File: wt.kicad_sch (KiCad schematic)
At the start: 59 parts, among them J1 USB_B, J2 Conn_ARM_JTAG_SWD_20, U1 STM32F407VGTx, Y1 Crystal_8Mhz

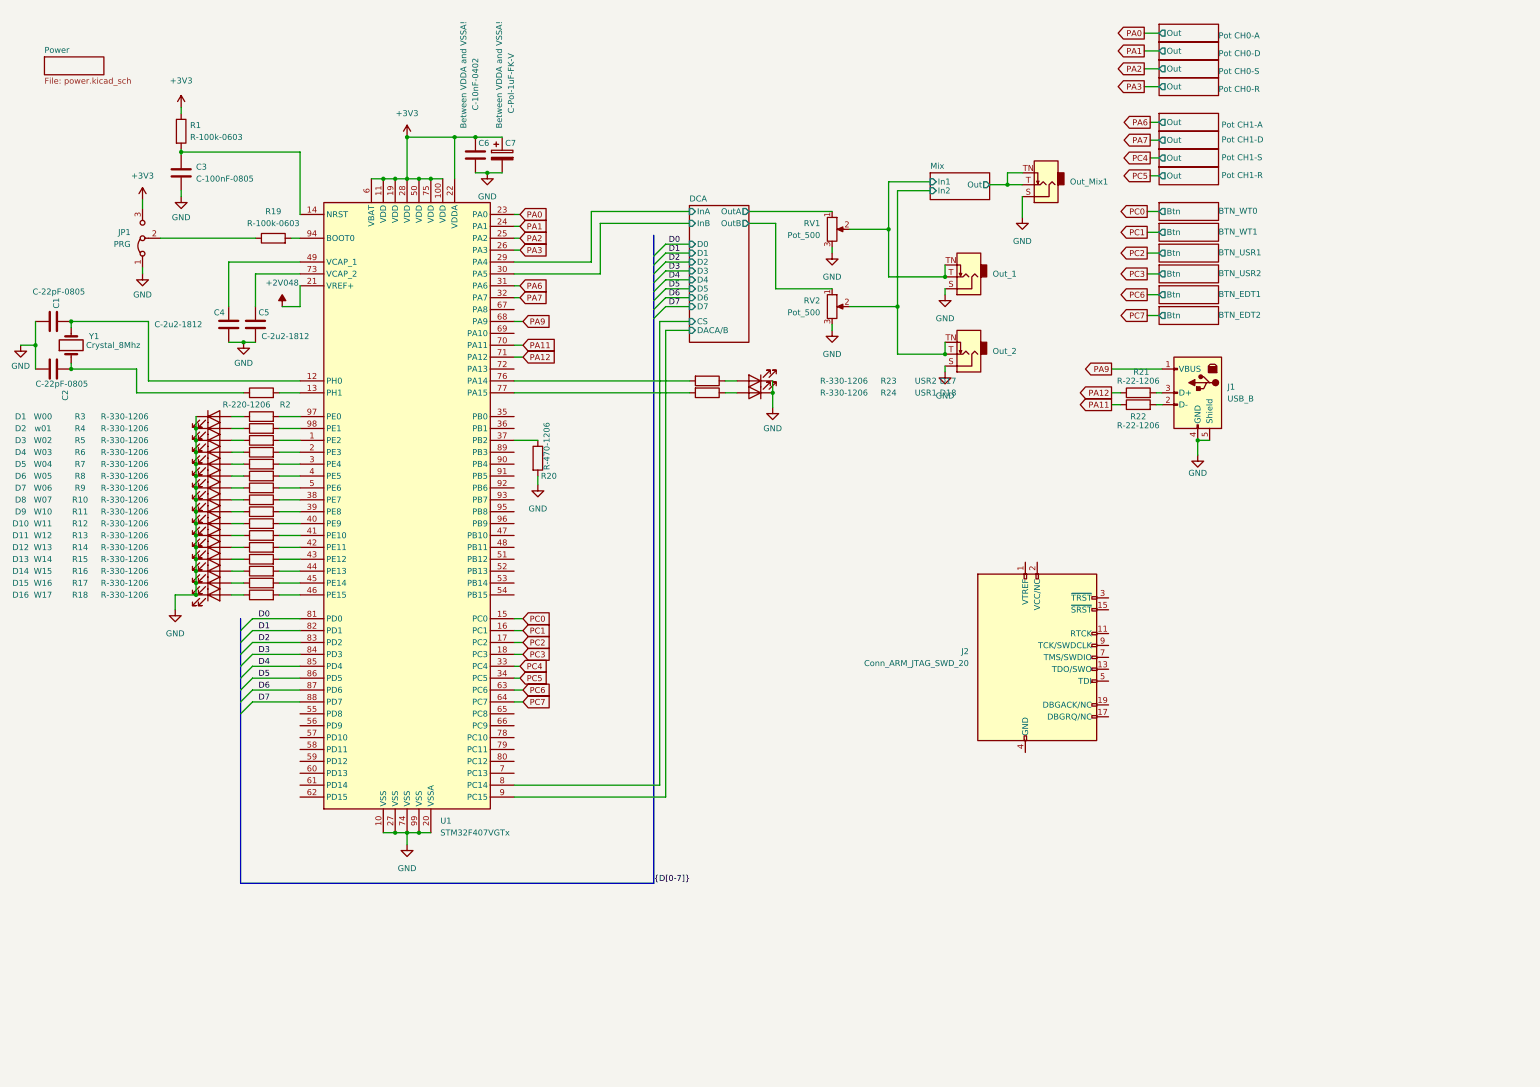
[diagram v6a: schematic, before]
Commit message: cleaning into modules
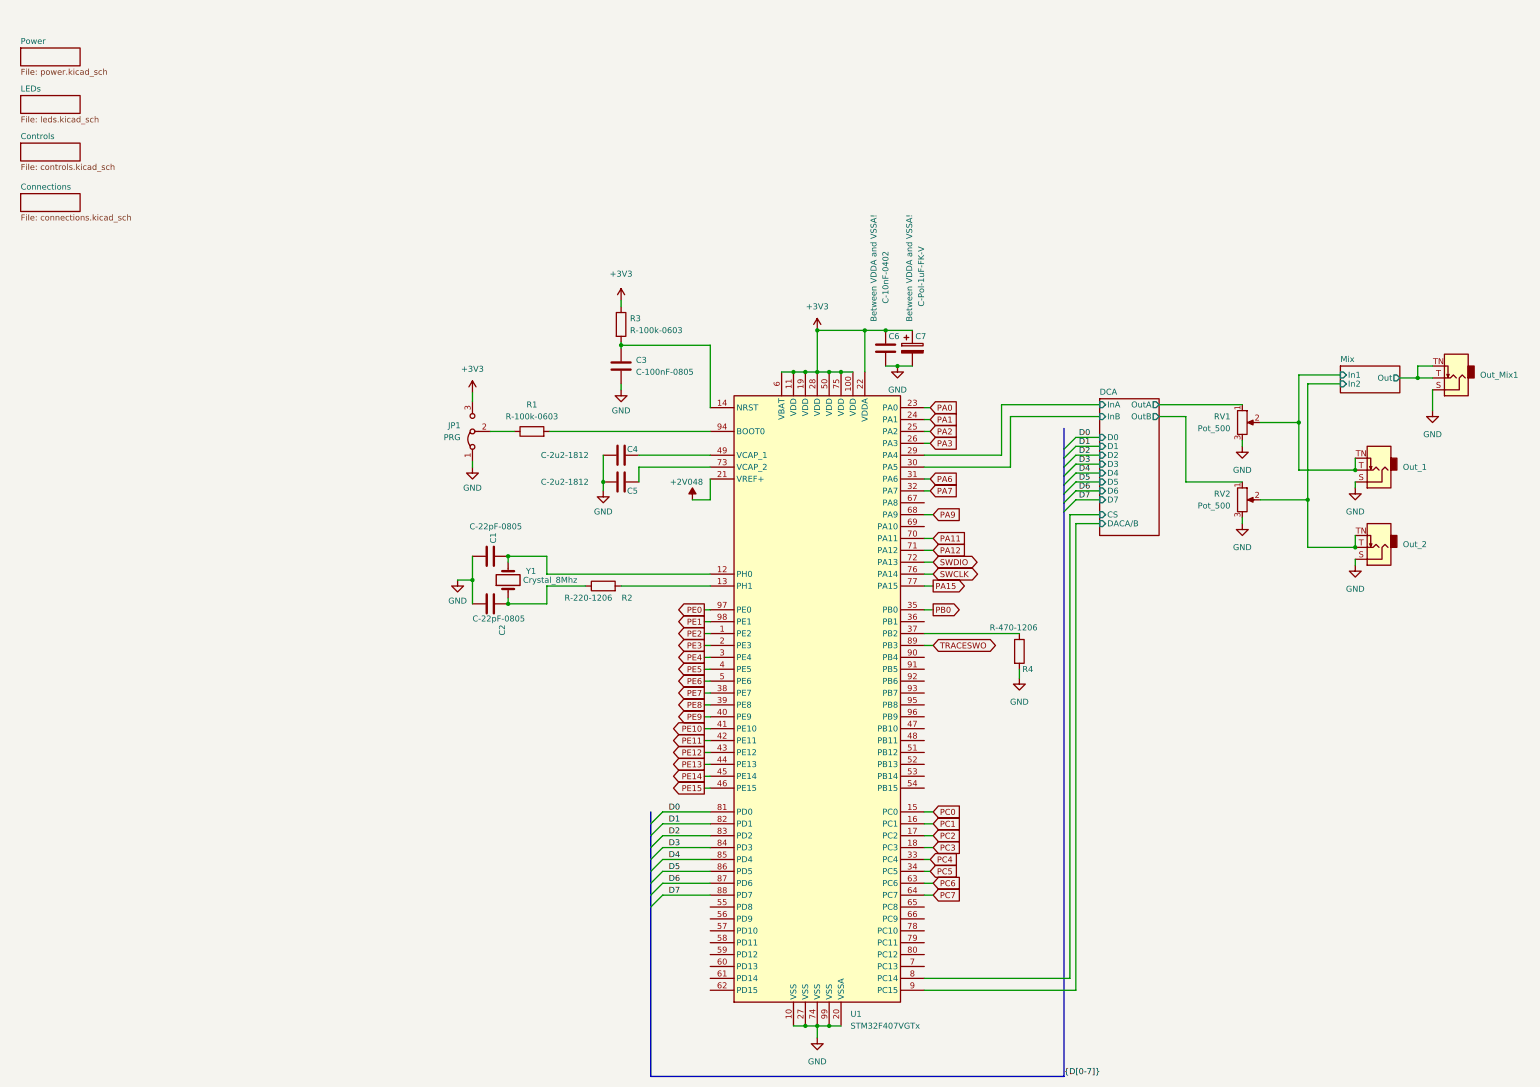
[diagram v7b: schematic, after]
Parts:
- removed D1: W00, Diode_SMD:D_1206_3216Metric_Pad1.42x1.75mm_HandSolder, symbol Device:LED
- removed D10: W11, Diode_SMD:D_1206_3216Metric_Pad1.42x1.75mm_HandSolder, symbol Device:LED
- removed D11: W12, Diode_SMD:D_1206_3216Metric_Pad1.42x1.75mm_HandSolder, symbol Device:LED
- removed D12: W13, Diode_SMD:D_1206_3216Metric_Pad1.42x1.75mm_HandSolder, symbol Device:LED
- removed D13: W14, Diode_SMD:D_1206_3216Metric_Pad1.42x1.75mm_HandSolder, symbol Device:LED
- removed D14: W15, Diode_SMD:D_1206_3216Metric_Pad1.42x1.75mm_HandSolder, symbol Device:LED
- removed D15: W16, Diode_SMD:D_1206_3216Metric_Pad1.42x1.75mm_HandSolder, symbol Device:LED
- removed D16: W17, Diode_SMD:D_1206_3216Metric_Pad1.42x1.75mm_HandSolder, symbol Device:LED
- removed D17: USR2, Diode_SMD:D_1206_3216Metric_Pad1.42x1.75mm_HandSolder, symbol Device:LED
- removed D18: USR1, Diode_SMD:D_1206_3216Metric_Pad1.42x1.75mm_HandSolder, symbol Device:LED
- removed D2: w01, Diode_SMD:D_1206_3216Metric_Pad1.42x1.75mm_HandSolder, symbol Device:LED
- removed D3: W02, Diode_SMD:D_1206_3216Metric_Pad1.42x1.75mm_HandSolder, symbol Device:LED
- removed D4: W03, Diode_SMD:D_1206_3216Metric_Pad1.42x1.75mm_HandSolder, symbol Device:LED
- removed D5: W04, Diode_SMD:D_1206_3216Metric_Pad1.42x1.75mm_HandSolder, symbol Device:LED
- removed D6: W05, Diode_SMD:D_1206_3216Metric_Pad1.42x1.75mm_HandSolder, symbol Device:LED
- removed D7: W06, Diode_SMD:D_1206_3216Metric_Pad1.42x1.75mm_HandSolder, symbol Device:LED
- removed D8: W07, Diode_SMD:D_1206_3216Metric_Pad1.42x1.75mm_HandSolder, symbol Device:LED
- removed D9: W10, Diode_SMD:D_1206_3216Metric_Pad1.42x1.75mm_HandSolder, symbol Device:LED
- removed J1: USB_B, eurorack:USB-BG, symbol eurorack:USB_B
- removed J2: Conn_ARM_JTAG_SWD_20, symbol Connector:Conn_ARM_JTAG_SWD_20
- removed R10, R11, R12, R13, R14, R15, R16, R17, R18, R23, R24, R3, R4, R5, R6, R7, R8, R9: R-330-1206, Resistor_SMD:R_1206_3216Metric_Pad1.30x1.75mm_HandSolder, symbol eurorack:R-330-1206
- removed R21, R22: R-22-1206, Resistor_SMD:R_1206_3216Metric_Pad1.30x1.75mm_HandSolder, symbol eurorack:R-22-1206
- JP1: footprint (none) -> Connector_PinSocket_2.54mm:PinSocket_1x03_P2.54mm_Vertical
- renumbered R19 to R1, R1 to R3, R20 to R4
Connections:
- net PE9: now reaches U1.40 (PE9)
- net PE3: now reaches U1.2 (PE3)
- net PA15: now reaches U1.77 (PA15)
- net PE8: now reaches U1.39 (PE8)
- net PE2: now reaches U1.1 (PE2)
- net PE4: now reaches U1.3 (PE4)
- net PB0: now reaches U1.35 (PB0)
- net PE7: now reaches U1.38 (PE7)
- net PE5: now reaches U1.4 (PE5)
- net PE10: now reaches U1.41 (PE10)
- net PE11: now reaches U1.42 (PE11)
- net PE12: now reaches U1.43 (PE12)
- net PE13: now reaches U1.44 (PE13)
- net PE14: now reaches U1.45 (PE14)
- net PE15: now reaches U1.46 (PE15)
- net PE6: now reaches U1.5 (PE6)
- net SWDIO: now reaches U1.72 (PA13)
- net SWCLK: now reaches U1.76 (PA14)
- net TRACESWO: now reaches U1.89 (PB3)
- net PE0: now reaches U1.97 (PE0)
- net PE1: now reaches U1.98 (PE1)
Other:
- removed sheet BTN_EDT1
- removed sheet BTN_EDT2
- removed sheet BTN_USR1
- removed sheet BTN_USR2
- removed sheet BTN_WT0
- removed sheet BTN_WT1
- removed sheet Pot CH0-A
- removed sheet Pot CH0-D
- removed sheet Pot CH0-R
- removed sheet Pot CH0-S
- removed sheet Pot CH1-A
- removed sheet Pot CH1-D
- removed sheet Pot CH1-R
- removed sheet Pot CH1-S
- added sheet Connections (connections.kicad_sch)
- added sheet Controls (controls.kicad_sch)
- added sheet LEDs (leds.kicad_sch)
- moved on the sheet: C1, C2, C3, C4, C5, C6, C7, JP1, Out_1, Out_2, Out_Mix1, R1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

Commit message: Working on the limiter
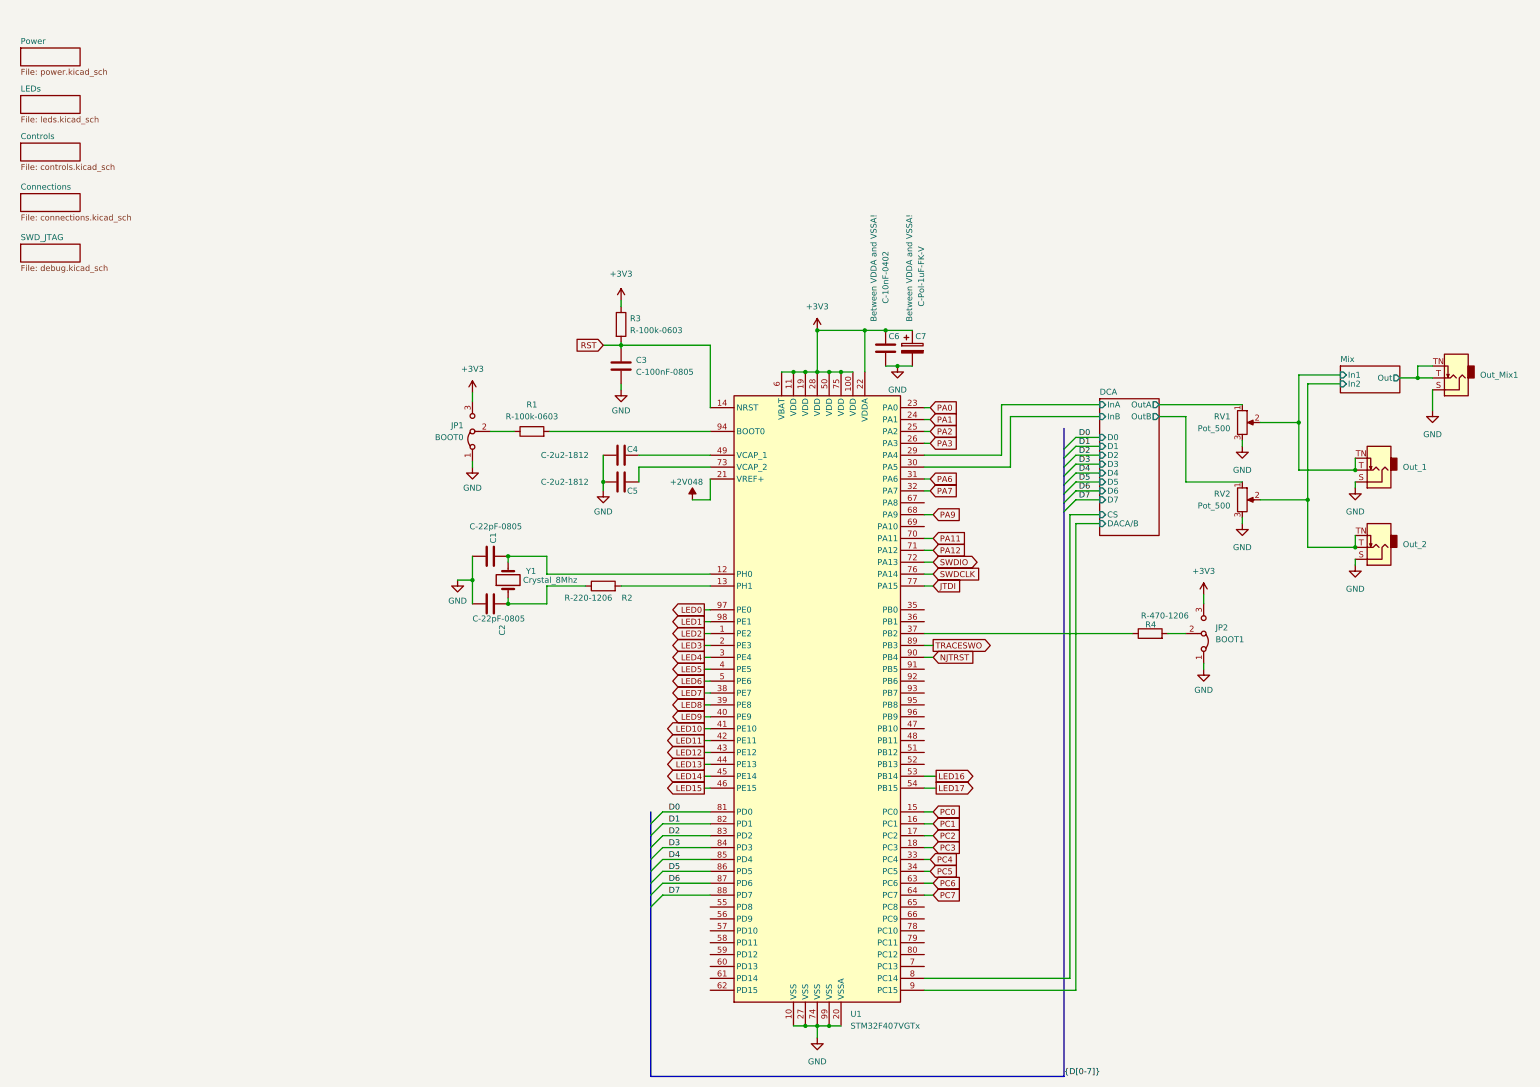
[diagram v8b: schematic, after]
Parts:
- added JP2: BOOT1, Connector_PinSocket_2.54mm:PinSocket_1x03_P2.54mm_Vertical, symbol Jumper:Jumper_3_Bridged12
- JP1: value PRG -> BOOT0
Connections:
- net +3V3: now also JP2.3 (B)
- net GND: now also JP2.1 (A); no longer R4.2
- net RST: now reaches C3.1, R3.2, U1.14 (NRST)
- net LED16: now reaches U1.53 (PB14)
- net LED17: now reaches U1.54 (PB15)
- net NJTRST: now reaches U1.90 (PB4)
- net PA15 renamed JTDI
- net PB0: no longer names the net of U1.35 (PB0)
- net PE0 renamed LED0
- net PE1 renamed LED1
- net PE10 renamed LED10
- net PE11 renamed LED11
- net PE12 renamed LED12
- net PE13 renamed LED13
- net PE14 renamed LED14
- net PE15 renamed LED15
- net PE2 renamed LED2
- net PE3 renamed LED3
- net PE4 renamed LED4
- net PE5 renamed LED5
- net PE6 renamed LED6
- net PE7 renamed LED7
- net PE8 renamed LED8
- net PE9 renamed LED9
- net SWCLK renamed SWDCLK
- new net: JP2.2 (C), R4.2
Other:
- added sheet SWD_JTAG (debug.kicad_sch)
- moved on the sheet: R4
